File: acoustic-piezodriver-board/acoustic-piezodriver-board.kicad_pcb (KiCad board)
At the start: 4 copper layers, 99 x 90 mm, 158 parts, among them J301 Conn_02x06_Odd_Even, J501 Conn_02x06_Odd_Even, P101 WJ128V-5.0-3P, P201 WJ128V-5.0-3P, Q501 AO3400A, Q502 AO3400A, U10 NCE6005AS, U101 AMS1117-3.3, U102 TMCS1108A3UQDR, U201 UCC27282DR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

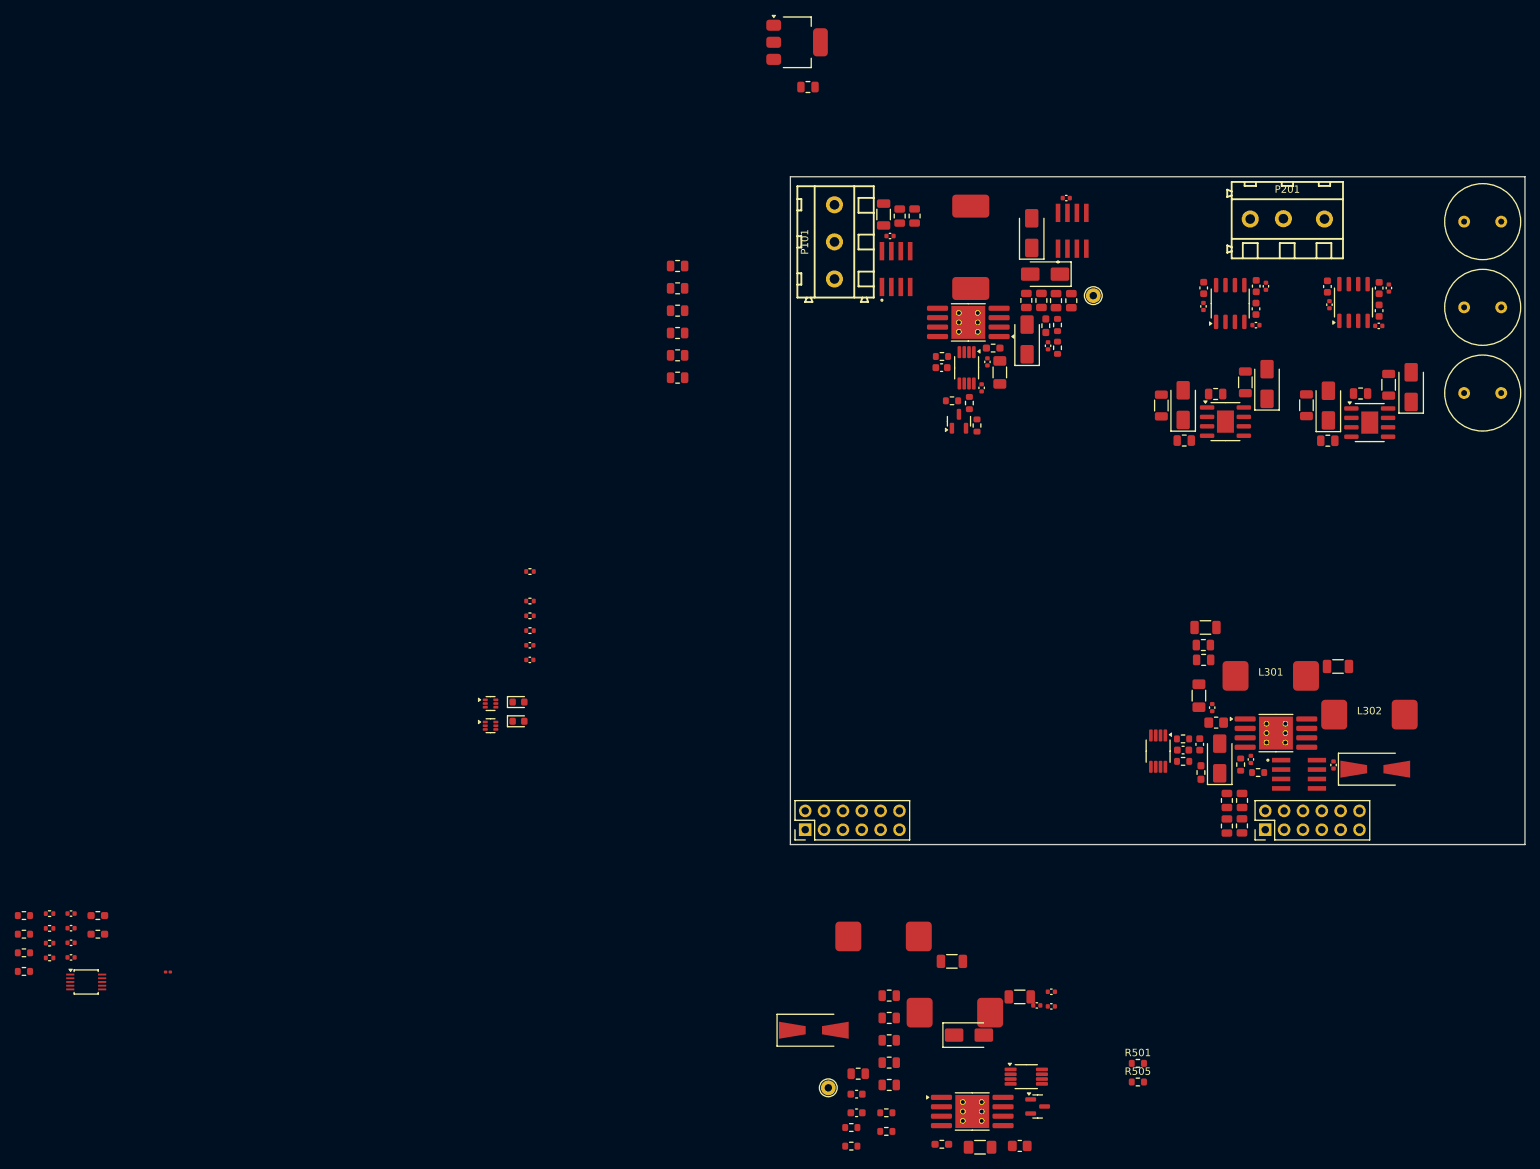
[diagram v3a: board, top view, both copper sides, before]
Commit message: rough layout completed, reduce board size and place components accordingly
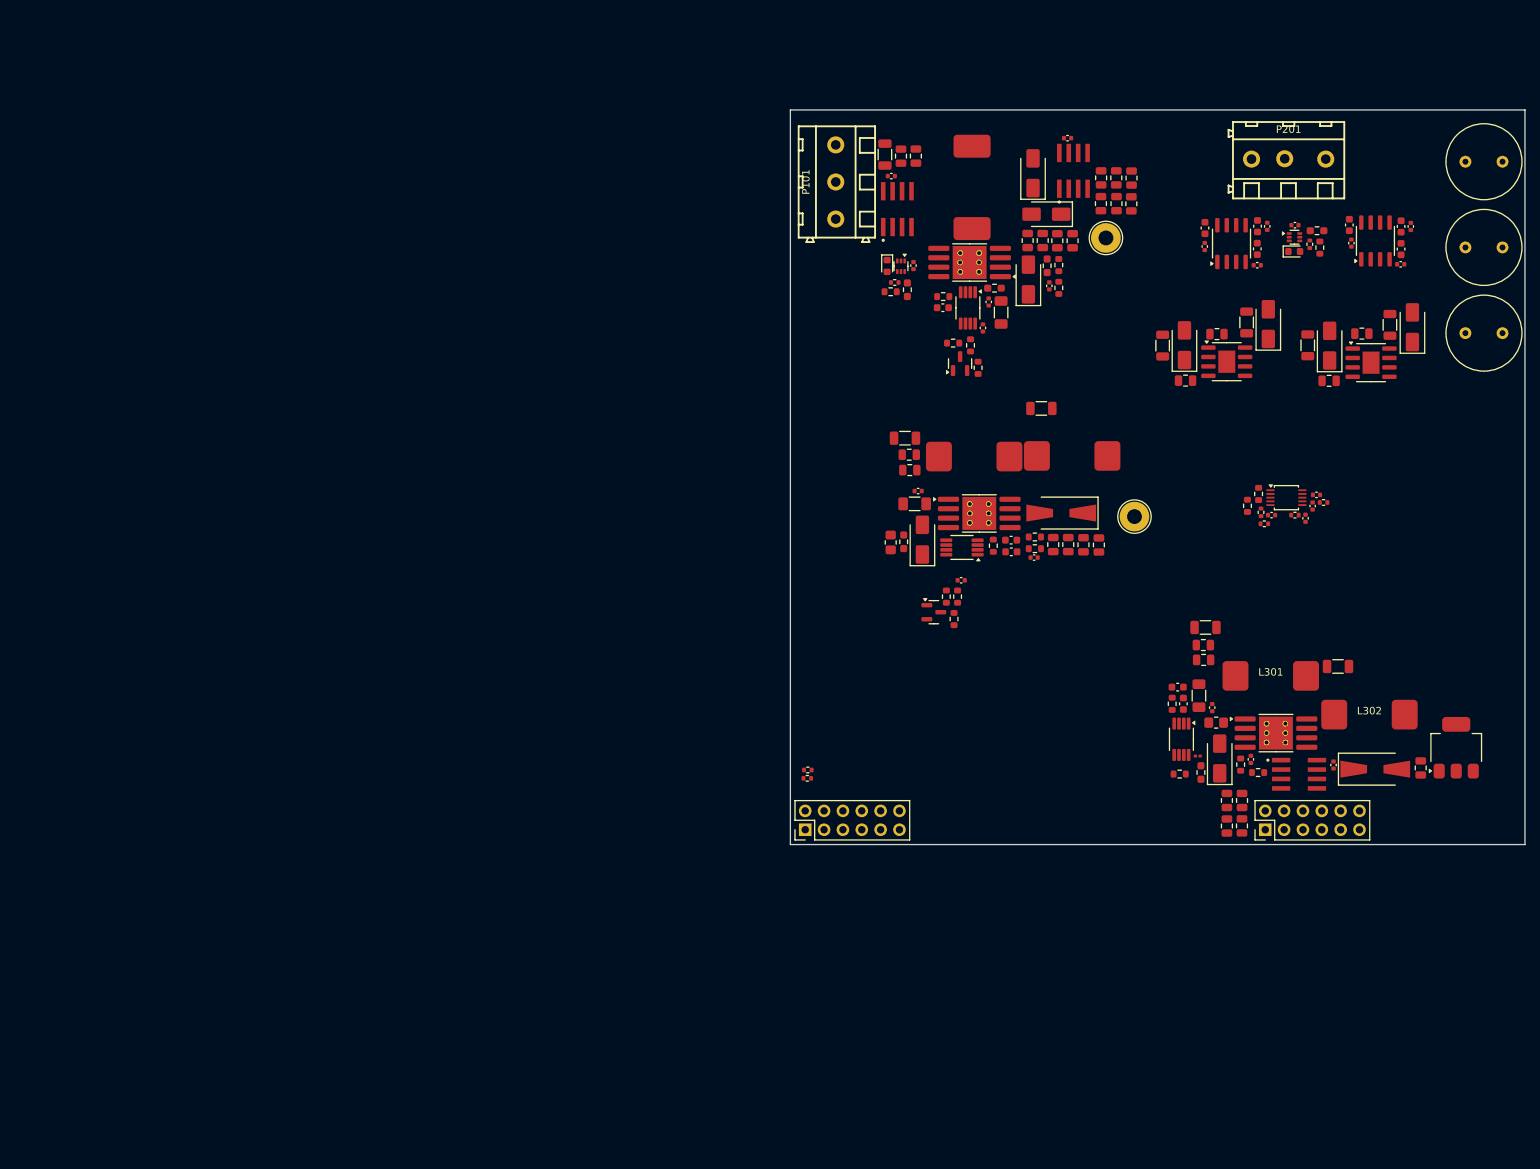
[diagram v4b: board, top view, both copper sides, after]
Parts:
- TP501, TP502: footprint TestPoint:TestPoint_THTPad_D2.0mm_Drill1.0mm -> TestPoint:TestPoint_THTPad_D4.0mm_Drill2.0mm
- moved R407 196.5 mm to (116.3, 61.5), turned to 90 degrees
- moved R406 189.7 mm to (116.0, 59.3), turned to 180 degrees
- moved R414 182.3 mm to (116.9, 95.9), turned to 180 degrees
- moved C406 178.0 mm to (115.4, 96.4), turned to -90 degrees
- moved C404 177.7 mm to (115.9, 94.9)
- moved R411 177.5 mm to (108.1, 94.8), turned to 90 degrees
- moved R410 176.8 mm to (113.0, 97.6)
- moved R412 176.4 mm to (106.6, 96.3), turned to 90 degrees
- moved C405 175.9 mm to (114.4, 98.0), turned to -90 degrees
- moved U404 174.4 mm to (111.8, 95.2)
- moved R413 173.3 mm to (108.4, 97.2), turned to 90 degrees
- moved R409 171.9 mm to (108.9, 98.8)
- moved C402 170.5 mm to (109.8, 97.6)
- moved R408 145.4 mm to (58.5, 67.5)
- moved C301 141.8 mm to (99.9, 130.1)
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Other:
- board size 99 x 90 mm -> 99 x 99 mm

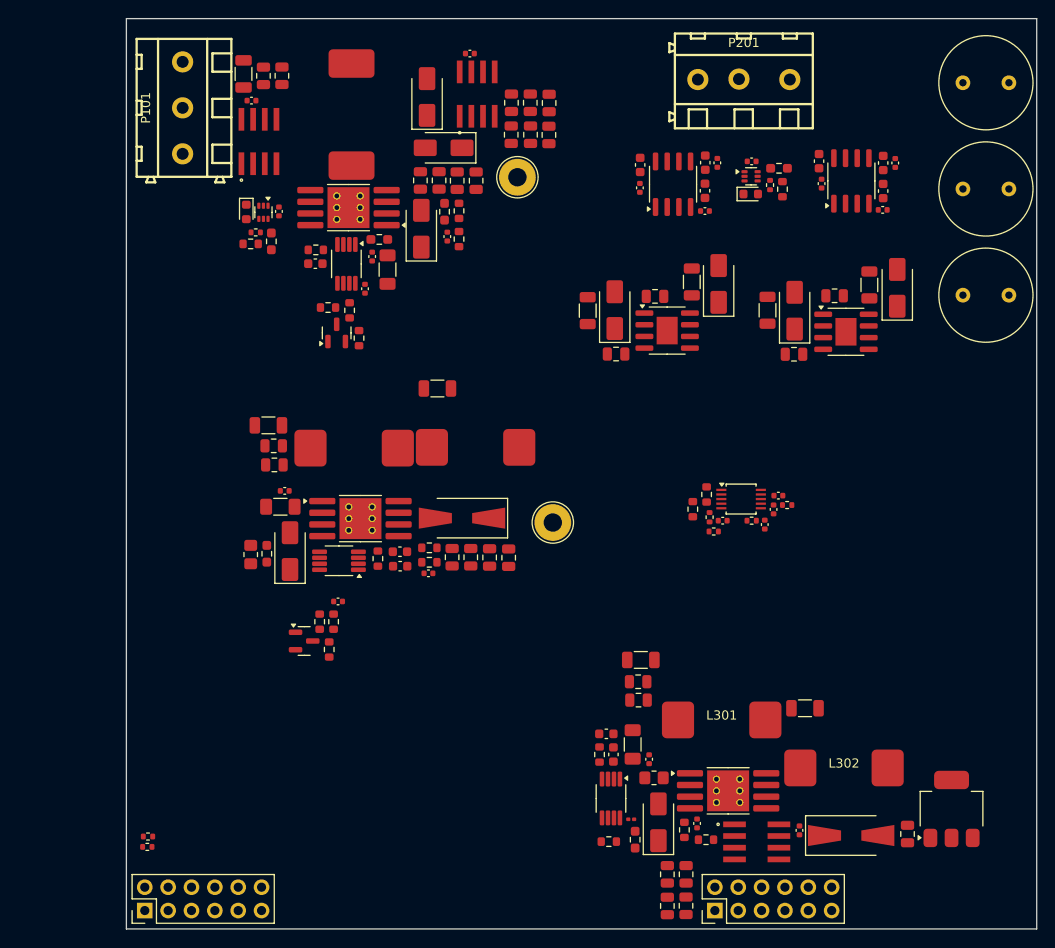
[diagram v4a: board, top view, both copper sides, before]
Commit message: completed positioning (next) routing
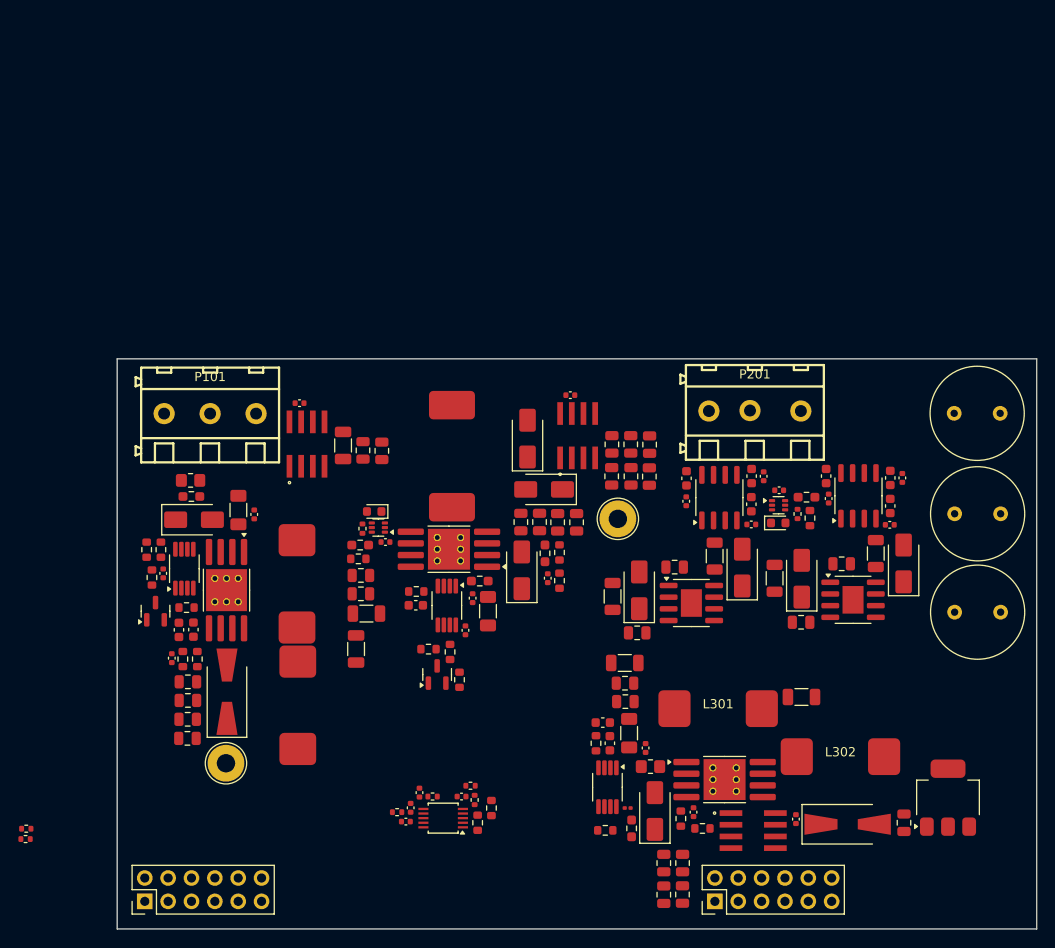
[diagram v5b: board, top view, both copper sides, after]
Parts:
- moved C201 57.6 mm to (135.1, 107.5)
- moved C514 57.3 mm to (70.5, 105.6), turned to 0 degrees
- moved R414 54.0 mm to (74.4, 129.3), turned to 0 degrees
- moved C404 53.8 mm to (75.4, 130.3), turned to 180 degrees
- moved C406 51.1 mm to (75.9, 128.8), turned to 90 degrees
- moved C405 47.5 mm to (76.9, 127.2), turned to 90 degrees
- moved U404 47.5 mm to (79.5, 129.9), turned to 180 degrees
- moved R410 45.9 mm to (78.3, 127.6), turned to 180 degrees
- moved TP502 44.1 mm to (55.8, 124.0), turned to -90 degrees
- moved R411 43.5 mm to (83.2, 130.4), turned to -90 degrees
- moved C515 42.2 mm to (72.8, 90.0)
- moved C513 41.8 mm to (68.6, 89.4)
- moved C402 41.3 mm to (81.5, 127.6), turned to 180 degrees
- moved C505 40.1 mm to (51.6, 121.3), turned to 180 degrees
- moved R413 40.0 mm to (82.9, 128.0), turned to -90 degrees
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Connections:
- P101 pad 1: Net-(P101-Pad1) -> GND
- P101 pad 2: GND -> Net-(P101-Pad2)
- P101 pad 3: GND -> Net-(P101-Pad2)
- P201 pad 2: /INVERTER/INV_LOADN -> GND
- P201 pad 3: GND -> /INVERTER/INV_LOADN
- U102 pad 1: Net-(P101-Pad1) -> Net-(P101-Pad2)
- U102 pad 2: Net-(P101-Pad1) -> Net-(P101-Pad2)
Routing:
- added copper zone on In2.Cu, net +BATT
- added copper zone on In1.Cu, net GND
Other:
- board size 99 x 99 mm -> 100 x 62 mm

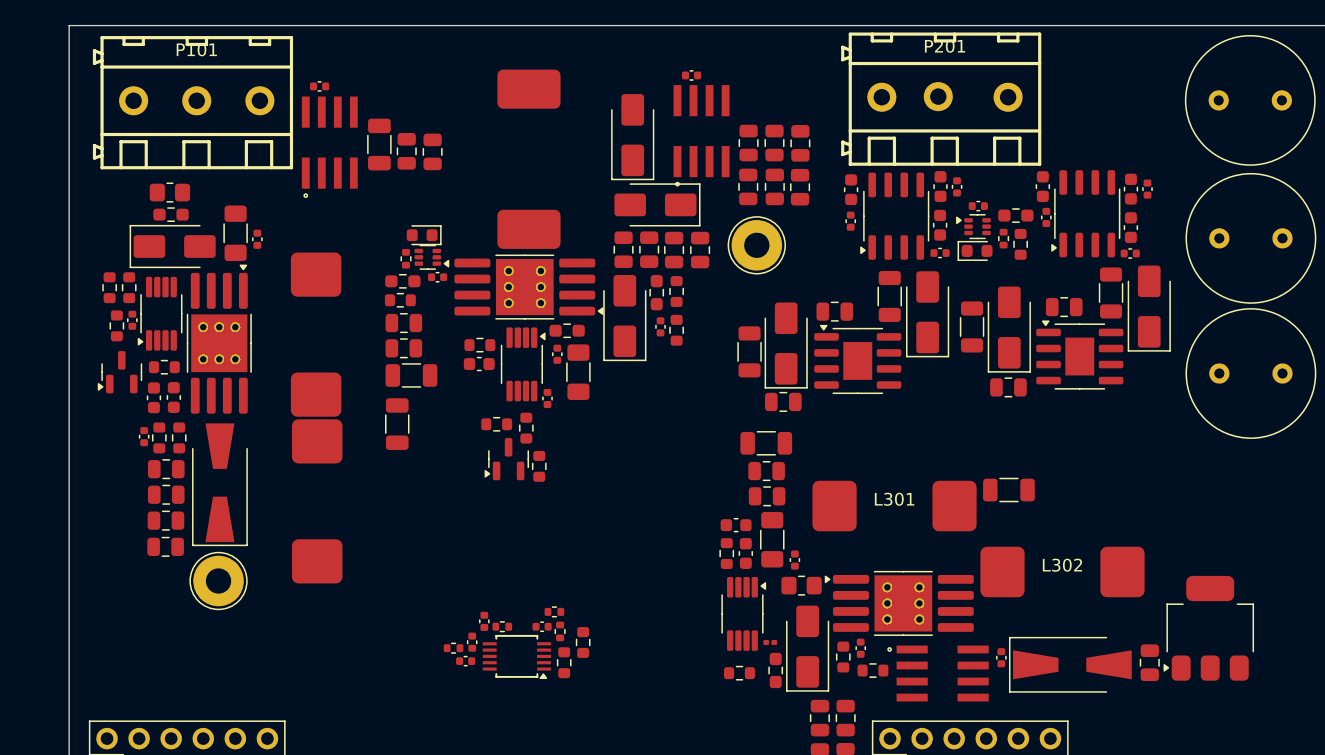
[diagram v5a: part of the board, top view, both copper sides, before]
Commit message: Did partial layout of inverter + 40 V boost + 10 V buck (next) Finish inverter, reorder and route SEPIC, check I2C bus capacitance limit
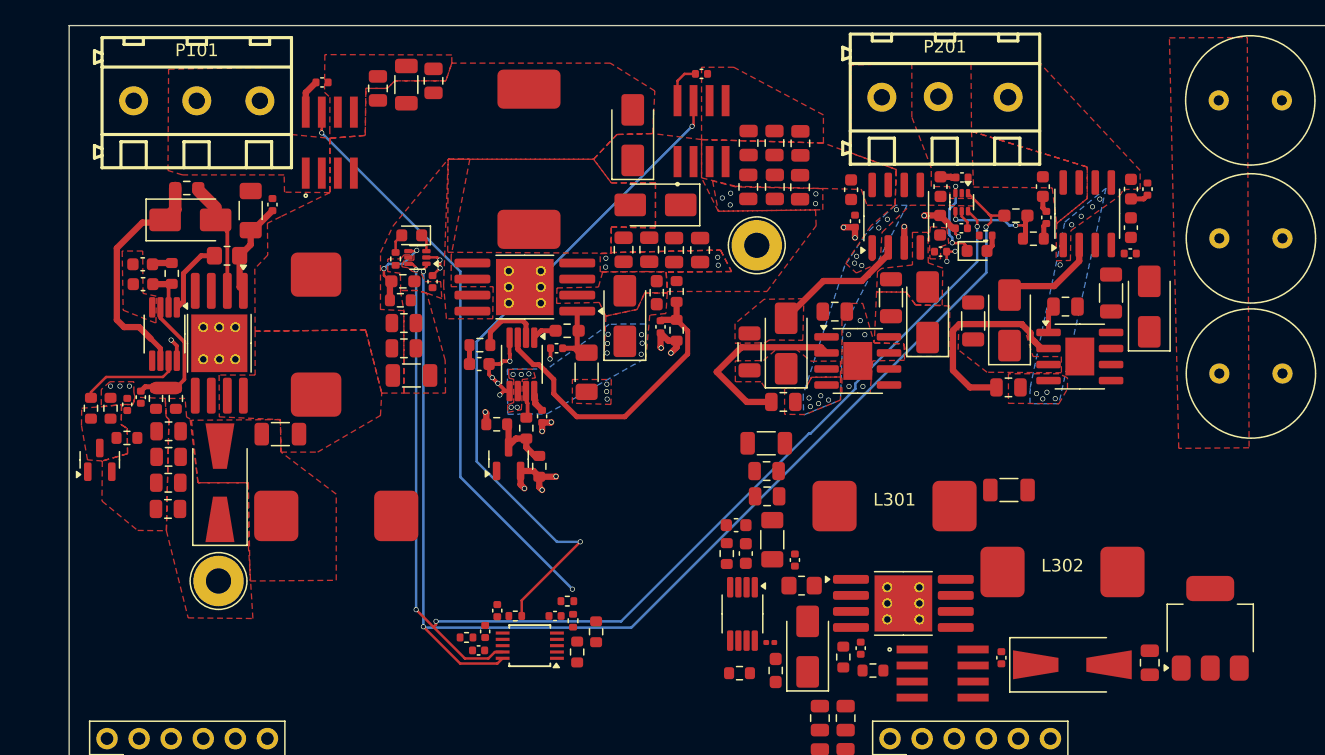
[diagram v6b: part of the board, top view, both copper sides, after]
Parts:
- U102: value TMCS1108A3UQDR -> D0008A-IPC_A
- moved C509 10.6 mm to (49.8, 98.9), turned to 180 degrees
- moved R501 9.66 mm to (47.3, 110.3)
- moved R505 9.66 mm to (45.7, 110.3)
- moved C512 9.30 mm to (49.9, 100.5), turned to 180 degrees
- moved C504 9.29 mm to (60.7, 112.3), turned to 180 degrees
- moved R504 8.91 mm to (48.6, 112.7), turned to 180 degrees
- moved R506 7.45 mm to (52.1, 99.6), turned to -90 degrees
- moved Q501 7.16 mm to (46.4, 114.4)
- moved R507 6.74 mm to (56.5, 98.2)
- moved C523 6.68 mm to (48.6, 110.0)
- moved C515 5.63 mm to (72.8, 84.4)
- moved C503 5.48 mm to (68.5, 85.0)
- moved C513 5.20 mm to (70.7, 84.7)
- moved C511 3.14 mm to (49.7, 109.4)
- moved R503 3.14 mm to (52.5, 109.5)
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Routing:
- net /SENSORS_CONN/T_SCL: track 0.00 -> 101.2 mm, vias 0 -> 3
- net /SENSORS_CONN/T_SDA: track 0.00 -> 96.2 mm, vias 0 -> 4
- net /INVERTER/ADC_IINV: track 0.00 -> 56.3 mm, vias 0 -> 2
- net /ADC_IBAT: track 0.00 -> 46.0 mm, vias 0 -> 2
- net GND: track 0.00 -> 31.8 mm, vias 0 -> 38
- net Net-(U504-FB): track 0.00 -> 25.1 mm
- net Net-(D503-K): track 0.00 -> 17.4 mm
- net Net-(U201-HB): track 0.00 -> 15.9 mm
- net Net-(U202-HB): track 0.00 -> 15.0 mm
- net Net-(D8-A): track 0.00 -> 10.7 mm
- net Net-(U502-FB): track 0.00 -> 10.4 mm
- net Net-(U403-ADD0): track 0.00 -> 9.09 mm, vias 0 -> 2
- net Net-(U502-FA/SD): track 0.00 -> 8.12 mm
- net Net-(D503-A): track 0.00 -> 7.95 mm
- net Net-(D11-A): track 0.00 -> 7.91 mm
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- added copper zone on F.Cu, net +3V3
- added copper zone on F.Cu, net +BATT
- added copper zone on F.Cu, net /INVERTER/10V
- added copper zone on B.Cu, net /INVERTER/INV_LOADN
- added copper zone on F.Cu, net /INVERTER/INV_LOADN
- added copper zone on B.Cu, net /INVERTER/INV_LOADP
- added copper zone on F.Cu, net /INVERTER/INV_LOADP
- added copper zone on F.Cu, net /INVERTER/VINV_N
- added copper zone on F.Cu, net /INVERTER/VINV_P
- added copper zone on F.Cu, net GND
- added copper zone on F.Cu, net Net-(C504-Pad1)
- added copper zone on F.Cu, net Net-(C9-Pad2)
- added copper zone on F.Cu, net Net-(D11-K)
- added copper zone on F.Cu, net Net-(D502-A)
- added copper zone on F.Cu, net Net-(D504-A)
- added copper zone on F.Cu, net Net-(D505-A)
- added copper zone on B.Cu, net Net-(D505-K)
- added copper zone on F.Cu, net Net-(D505-K)
- added copper zone on F.Cu, net Net-(D8-A)
- added copper zone on F.Cu, net Net-(D8-K)
- added copper zone on F.Cu, net Net-(D9-A)
- added copper zone on F.Cu, net Net-(D9-K)
- added copper zone on F.Cu, net Net-(P101-Pad2)
- added copper zone on F.Cu, net Net-(Q501-D)
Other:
- board text added: "Routed driver on lower layer to avoid coupling of driver current into feedback path"
